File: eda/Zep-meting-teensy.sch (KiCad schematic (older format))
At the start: 10 parts, among them P1 CONN_01X03, U3 Teensy3.2, U5 TEMT6000_sparkfun, U6 LM358N

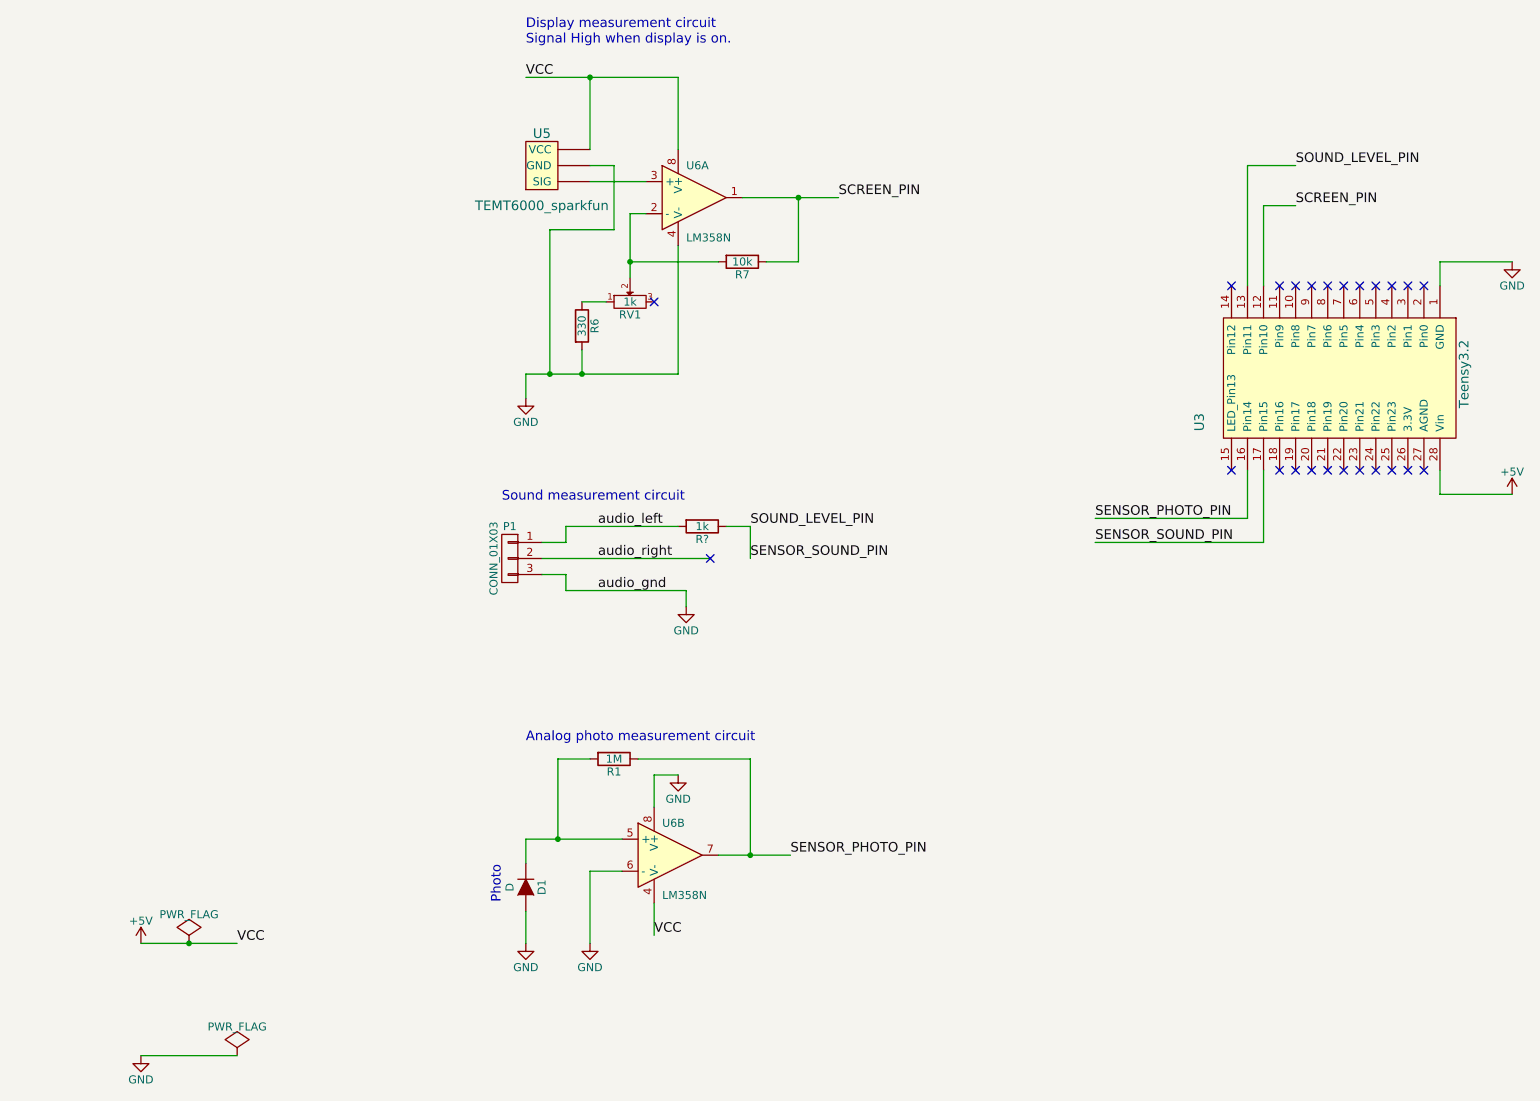
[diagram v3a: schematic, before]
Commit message: Update schematics, include standard parallel port
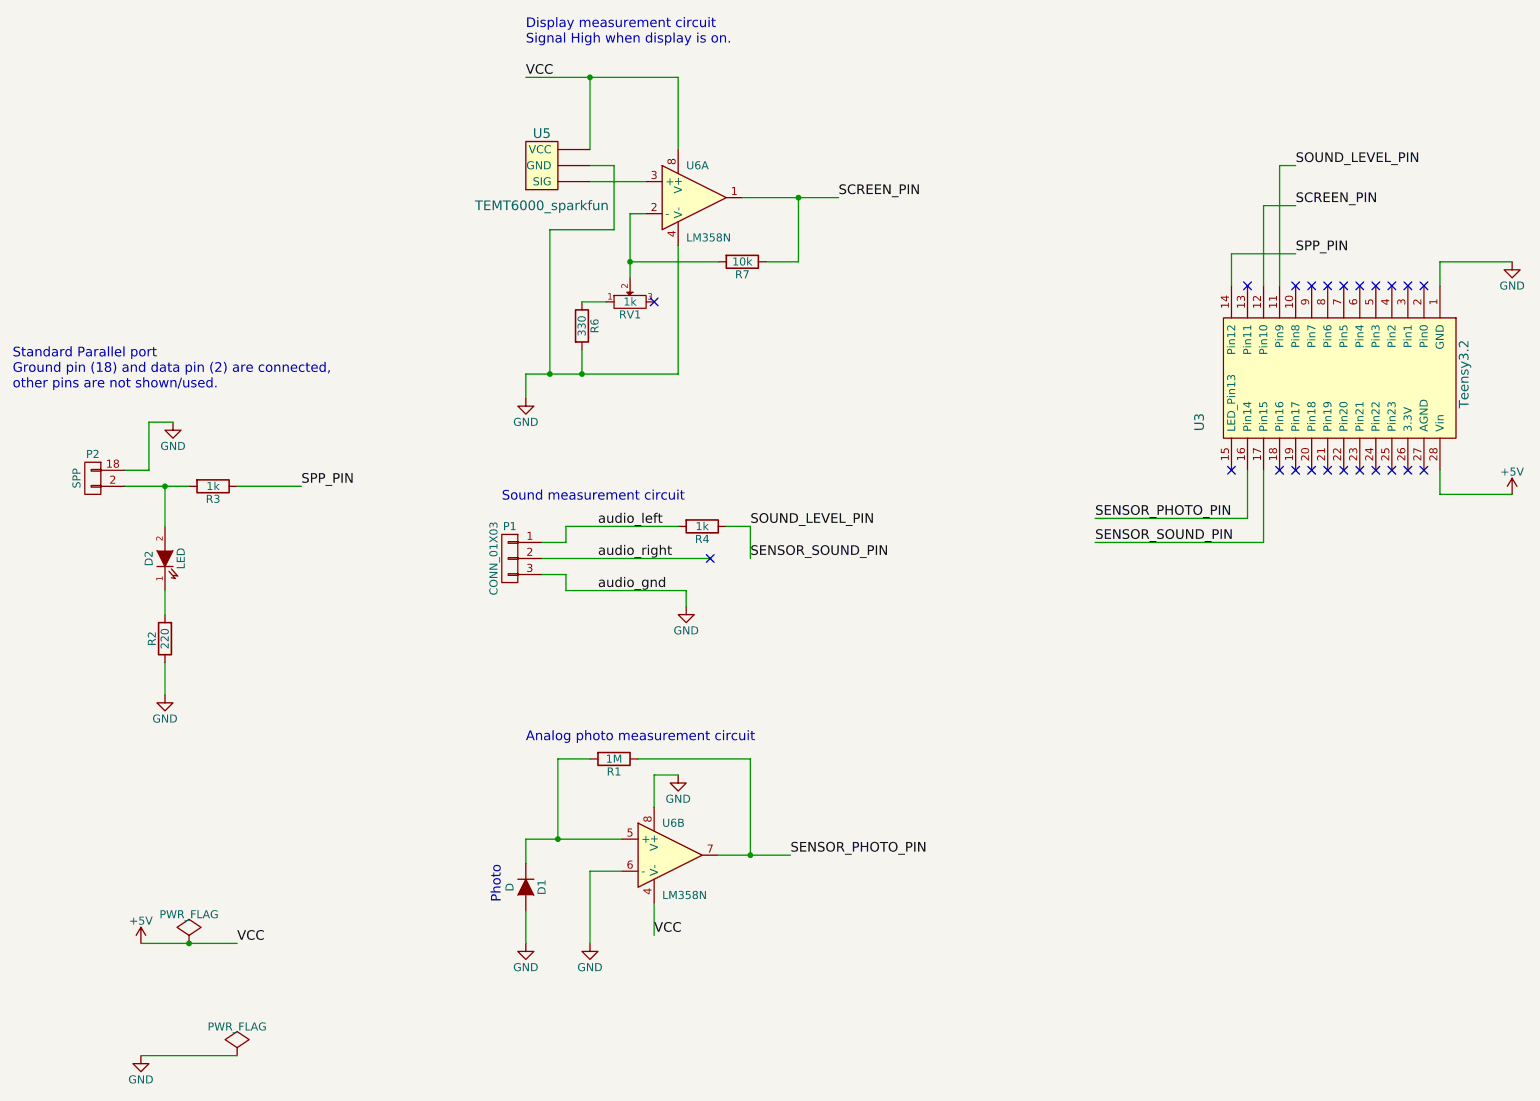
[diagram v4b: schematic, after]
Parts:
- added D2: LED, symbol LED
- added P2: SPP, symbol CONN_01X02
- added R2: 220, symbol R
- added R3: 1k, symbol R
- gave numbers to parts that had none: 1
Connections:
- net GND: now also P2.18 (P1), R2.1
- net SENSOR_SOUND_PIN: now also U3.11 (Pin9); no longer U3.13 (Pin11)
- net SPP_PIN: now reaches U3.14 (Pin12)
- net SPP_PIN: now also R3.1
- new net: D2.2 (A), P2.2 (P2), R3.2
- new net: D2.1 (K), R2.2
- no-connect marks 24 -> 23
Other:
- note added: "Standard Parallel port \nGround pin (18) and data pin (2) are connected,\nother pins are not shown/used."
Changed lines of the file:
@@
 $EndDescr
 $Comp
-L +5V #PWR2
+L +5V #PWR1
 U 1 1 59254CF6
 P 1400 6350
-F 0 "#PWR2" H 1400 6200 50  0001 C CNN
+F 0 "#PWR1" H 1400 6200 50  0001 C CNN
 F 1 "+5V" H 1400 6490 50  0000 C CNN
 F 2 "" H 1400 6350 50  0000 C CNN
@@
 $EndComp
 $Comp
-L GND #PWR3
+L GND #PWR2
 U 1 1 59254D0A
 P 1400 7050
-F 0 "#PWR3" H 1400 6800 50  0001 C CNN
+F 0 "#PWR2" H 1400 6800 50  0001 C CNN
 F 1 "GND" H 1400 6900 50  0000 C CNN
 F 2 "" H 1400 7050 50  0000 C CNN
@@
 NoConn ~ 9300 3400
 NoConn ~ 9400 3400
-NoConn ~ 8500 2250
 NoConn ~ 8600 2250
 NoConn ~ 8700 2250
@@
 audio_left
 $Comp
-L GND #PWR8
+L GND #PWR9
 U 1 1 5931661E
 P 4800 4250
-F 0 "#PWR8" H 4800 4000 50  0001 C CNN
+F 0 "#PWR9" H 4800 4000 50  0001 C CNN
 F 1 "GND" H 4800 4100 50  0000 C CNN
 F 2 "" H 4800 4250 50  0000 C CNN
@@
 $EndComp
 $Comp
-L GND #PWR4
+L GND #PWR6
 U 1 1 59317642
 P 3800 6350
-F 0 "#PWR4" H 3800 6100 50  0001 C CNN
+F 0 "#PWR6" H 3800 6100 50  0001 C CNN
 F 1 "GND" H 3800 6200 50  0000 C CNN
 F 2 "" H 3800 6350 50  0000 C CNN
@@
 $EndComp
 $Comp
-L GND #PWR6
+L GND #PWR7
 U 1 1 5931780C
 P 4200 6350
-F 0 "#PWR6" H 4200 6100 50  0001 C CNN
+F 0 "#PWR7" H 4200 6100 50  0001 C CNN
 F 1 "GND" H 4200 6200 50  0000 C CNN
 F 2 "" H 4200 6350 50  0000 C CNN
@@
 	9500 2100 9950 2100
 Wire Wire Line
-	8400 2250 8400 1750
-Wire Wire Line
 	8400 1750 8600 1750
 Wire Wire Line
-	8300 2250 8300 1500
-Wire Wire Line
-	8300 1500 8600 1500
+	8500 1500 8600 1500
 Wire Wire Line
 	3900 4050 4050 4050
@@
 	4600 5300 4750 5300
 $Comp
-L GND #PWR7
+L GND #PWR8
 U 1 1 593179DE
 P 4750 5300
-F 0 "#PWR7" H 4750 5050 50  0001 C CNN
+F 0 "#PWR8" H 4750 5050 50  0001 C CNN
 F 1 "GND" H 4750 5150 50  0000 C CNN
 F 2 "" H 4750 5300 50  0000 C CNN
@@
 	1400 6350 2000 6350
 Connection ~ 1700 6350
-NoConn ~ 8200 2250
 $Comp
 L POT RV1
@@
 Connection ~ 4200 950
 $Comp
-L GND #PWR1
+L GND #PWR5
 U 1 1 594BD15B
 P 3800 2950
-F 0 "#PWR1" H 3800 2700 50  0001 C CNN
+F 0 "#PWR5" H 3800 2700 50  0001 C CNN
 F 1 "GND" H 3800 2800 50  0000 C CNN
 F 2 "" H 3800 2950 50  0000 C CNN
@@
 NoConn ~ 4950 3950
 $Comp
-L R R?
+L R R4
 U 1 1 59C2429A
 P 4900 3750
-F 0 "R?" V 4980 3750 50  0000 C CNN
+F 0 "R4" V 4980 3750 50  0000 C CNN
 F 1 "1k" V 4900 3750 50  0000 C CNN
 F 2 "" V 4830 3750 50  0000 C CNN
@@
 NoConn ~ 9200 3400
 NoConn ~ 9100 3400
+$Comp
+L CONN_01X02 P2
+U 1 1 59FC92BD
+P 1100 3450
+F 0 "P2" H 1100 3600 50  0000 C CNN
+F 1 "SPP" V 1200 3450 50  0000 C CNN
+F 2 "" H 1100 3450 50  0000 C CNN
+F 3 "" H 1100 3450 50  0000 C CNN
+	1    1100 3450
+	-1   0    0    -1
+$EndComp
+$Comp
+L R R3
+U 1 1 59FC99EA
+P 1850 3500
+F 0 "R3" V 1930 3500 50  0000 C CNN
+F 1 "1k" V 1850 3500 50  0000 C CNN
+F 2 "" V 1780 3500 50  0000 C CNN
+F 3 "" H 1850 3500 50  0000 C CNN
+	1    1850 3500
+	0    1    1    0
+$EndComp
+$Comp
+L LED D2
+U 1 1 59FC9A54
+P 1550 3950
+F 0 "D2" H 1550 4050 50  0000 C CNN
+F 1 "LED" H 1550 3850 50  0000 C CNN
+F 2 "" H 1550 3950 50  0000 C CNN
+F 3 "" H 1550 3950 50  0000 C CNN
+	1    1550 3950
+	0    -1   -1   0
+$EndComp
+Wire Wire Line
+	1300 3500 1700 3500
+Wire Wire Line
+	1550 3750 1550 3500
+Connection ~ 1550 3500
+$Comp
+L R R2
+U 1 1 59FC9B99
+P 1550 4450
+F 0 "R2" V 1630 4450 50  0000 C CNN
+F 1 "220" V 1550 4450 50  0000 C CNN
+F 2 "" V 1480 4450 50  0000 C CNN
+F 3 "" H 1550 4450 50  0000 C CNN
+	1    1550 4450
+	-1   0    0    1
+$EndComp
+$Comp
+L GND #PWR3
+U 1 1 59FCA26B
+P 1550 4800
+F 0 "#PWR3" H 1550 4550 50  0001 C CNN
+F 1 "GND" H 1550 4650 50  0000 C CNN
+F 2 "" H 1550 4800 50  0000 C CNN
+F 3 "" H 1550 4800 50  0000 C CNN
+	1    1550 4800
+	1    0    0    -1
+$EndComp
+Wire Wire Line
+	1550 4150 1550 4300
+Wire Wire Line
+	1550 4600 1550 4800
+$Comp
+L GND #PWR4
+U 1 1 59FCA373
+P 1600 3100
+F 0 "#PWR4" H 1600 2850 50  0001 C CNN
+F 1 "GND" H 1600 2950 50  0000 C CNN
+F 2 "" H 1600 3100 50  0000 C CNN
+F 3 "" H 1600 3100 50  0000 C CNN
+	1    1600 3100
+	1    0    0    -1
+$EndComp
+Wire Wire Line
+	1450 3400 1450 3100
+Wire Wire Line
+	1450 3100 1600 3100
+Wire Wire Line
+	2000 3500 2400 3500
+Text Label 2400 3500 0    60   ~ 0
+SPP_PIN
+Wire Wire Line
+	8400 1750 8400 2250
+Wire Wire Line
+	8500 1500 8500 2250
+NoConn ~ 8300 2250
+Wire Wire Line
+	8200 2250 8200 2050
+Wire Wire Line
+	8200 2050 8600 2050
+Text Label 8600 2050 0    60   ~ 0
+SPP_PIN
+Text Notes 600  2900 0    60   ~ 0
+Standard Parallel port \nGround pin (18) and data pin (2) are connected,\nother pins are not shown/used.
+Wire Wire Line
+	1450 3400 1300 3400
 $EndSCHEMATC
